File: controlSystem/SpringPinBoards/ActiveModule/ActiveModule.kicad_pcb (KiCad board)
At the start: 2 copper layers, 18.7 x 13.3 mm, 9 parts, among them J1 Conn_01x01_Male, J2 Conn_01x01_Male, J3 Conn_01x01_Male, J4 Conn_01x01_Male, J5 Conn_01x01_Male, J6 Conn_01x01_Male, J7 Conn_01x06

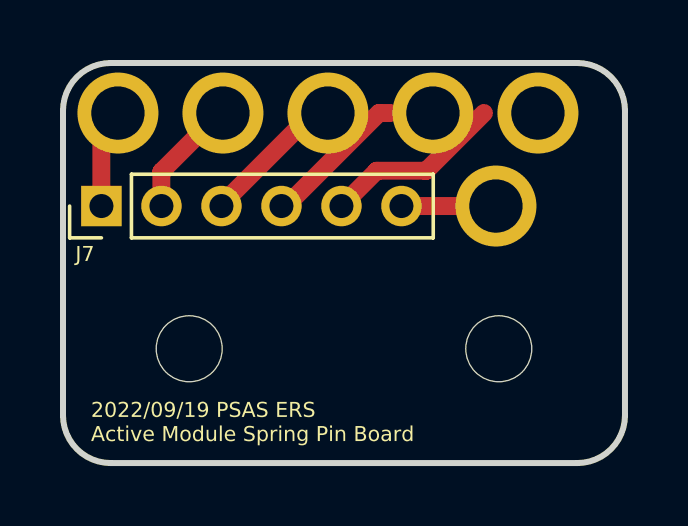
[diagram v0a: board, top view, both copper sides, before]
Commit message: Widened traces on the spring pin boards
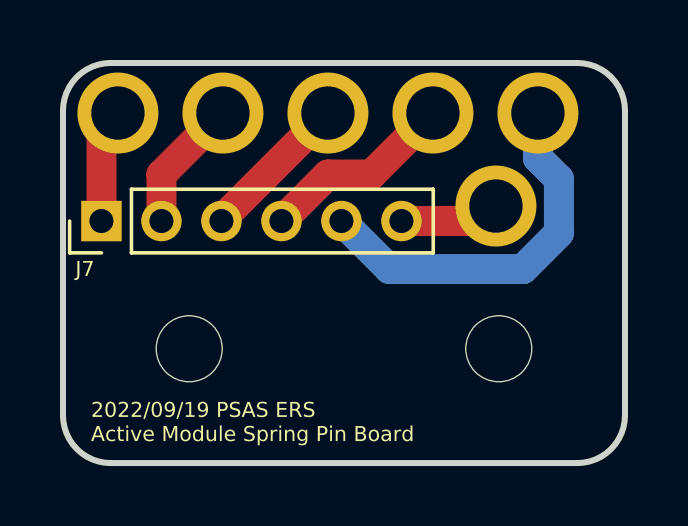
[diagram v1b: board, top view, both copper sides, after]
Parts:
- moved J7 0.50 mm to (141.2, 74.4)
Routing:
- net Net-(J5-Pad1): track 6.03 -> 12.7 mm
- net Net-(J4-Pad1): track 4.93 -> 6.54 mm
- net Net-(J3-Pad1): track 4.16 -> 5.07 mm
- net Net-(J2-Pad1): track 3.70 -> 4.45 mm
- net Net-(J1-Pad1): track 3.24 -> 3.83 mm
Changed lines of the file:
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@@
   (net 6 "Net-(J6-Pad1)")
   (footprint "Connector_PinHeader_2.00mm:PinHeader_1x06_P2.00mm_Vertical" (layer "F.Cu")
-    (at 141.25 73.9 90)
+    (at 141.25 74.4 90)
     (descr "Through hole straight pin header, 1x06, 2.00mm pitch, single row")
     (tags "Through hole pin header THT 1x06 2.00mm single row")
@@
     (effects (font (size 0.5 0.5) (thickness 0.12)) (justify left))
   )
-  (segment (start 141.25 73.9) (end 141.25 71.15) (width 0.6) (layer "F.Cu") (net 1))
-  (segment (start 141.25 71.15) (end 141.6 70.8) (width 0.6) (layer "F.Cu") (net 1))
-  (segment (start 143.25 72.75) (end 144.7 71.3) (width 0.6) (layer "F.Cu") (net 2))
-  (segment (start 143.25 73.9) (end 143.25 72.75) (width 0.6) (layer "F.Cu") (net 2))
-  (segment (start 144.7 71.3) (end 144.7 70.8) (width 0.6) (layer "F.Cu") (net 2))
-  (segment (start 147.8 71.3) (end 147.8 70.8) (width 0.6) (layer "F.Cu") (net 3))
-  (segment (start 145.25 73.85) (end 147.8 71.3) (width 0.6) (layer "F.Cu") (net 3))
-  (segment (start 145.25 73.9) (end 145.25 73.85) (width 0.6) (layer "F.Cu") (net 3))
-  (segment (start 147.25 73.9) (end 147.4 73.9) (width 0.6) (layer "F.Cu") (net 4))
-  (segment (start 150.5 70.8) (end 150.9 70.8) (width 0.6) (layer "F.Cu") (net 4))
-  (segment (start 147.4 73.9) (end 150.5 70.8) (width 0.6) (layer "F.Cu") (net 4))
-  (segment (start 149.25 73.9) (end 150.425 72.725) (width 0.6) (layer "F.Cu") (net 5))
-  (segment (start 152.075 72.725) (end 154 70.8) (width 0.6) (layer "F.Cu") (net 5))
-  (segment (start 150.425 72.725) (end 152.075 72.725) (width 0.6) (layer "F.Cu") (net 5))
-  (segment (start 151.25 73.9) (end 154.4 73.9) (width 0.6) (layer "F.Cu") (net 6))
+  (segment (start 141.25 71.35) (end 141.8 70.8) (width 1) (layer "F.Cu") (net 1))
+  (segment (start 141.25 74.4) (end 141.25 71.35) (width 1) (layer "F.Cu") (net 1))
+  (segment (start 143.25 72.85) (end 145.3 70.8) (width 1) (layer "F.Cu") (net 2))
+  (segment (start 143.25 74.4) (end 143.25 72.85) (width 1) (layer "F.Cu") (net 2))
+  (segment (start 145.25 74.4) (end 145.25 74.35) (width 1) (layer "F.Cu") (net 3))
+  (segment (start 145.25 74.35) (end 148.8 70.8) (width 1) (layer "F.Cu") (net 3))
+  (segment (start 148.8 72.85) (end 150.25 72.85) (width 1) (layer "F.Cu") (net 4))
+  (segment (start 147.25 74.4) (end 148.8 72.85) (width 1) (layer "F.Cu") (net 4))
+  (segment (start 150.25 72.85) (end 152.3 70.8) (width 1) (layer "F.Cu") (net 4))
+  (segment (start 150.85 76) (end 155.3 76) (width 1) (layer "B.Cu") (net 5))
+  (segment (start 155.3 76) (end 156.5 74.8) (width 1) (layer "B.Cu") (net 5))
+  (segment (start 156.5 74.8) (end 156.5 73) (width 1) (layer "B.Cu") (net 5))
+  (segment (start 155.8 72.3) (end 155.8 70.8) (width 1) (layer "B.Cu") (net 5))
+  (segment (start 156.5 73) (end 155.8 72.3) (width 1) (layer "B.Cu") (net 5))
+  (segment (start 149.25 74.4) (end 150.85 76) (width 1) (layer "B.Cu") (net 5))
+  (segment (start 151.25 74.4) (end 153.9 74.4) (width 1) (layer "F.Cu") (net 6))
+  (segment (start 153.9 74.4) (end 154.4 73.9) (width 1) (layer "F.Cu") (net 6))
   (group "" (id 67053cc4-faed-4cf5-96b7-90713502d4d0)
     (members

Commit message: Moved spring pin board libraries to psas-kicad
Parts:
- J1, J2, J3, J4, J5, J6: footprint Mill-Max-0921-5-15-20-77-14-11-0:0921-5-15-20-77-14-11-0 -> psas-footprints:Mill-Max-0921-5-15-20-77-14-11-0
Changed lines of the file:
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@@
     (pad "" np_thru_hole circle (at 0 0) (size 2.2 2.2) (drill 2.2) (layers *.Cu *.Mask))
   )
-  (footprint "Mill-Max-0921-5-15-20-77-14-11-0:0921-5-15-20-77-14-11-0" (layer "F.Cu")
+  (footprint "psas-footprints:Mill-Max-0921-5-15-20-77-14-11-0" (layer "F.Cu")
     (at 154.4 73.9)
     (property "Sheetfile" "ActiveModule.kicad_sch")
@@
       (rotate (xyz 0 90 0))
     )
+    (model "${PSAS_LIBRARIES}/psas-3dmodels/mill-max-0921-5-15-20-77-14-11-0 .step"
+      (offset (xyz 0 0 -3.5))
+      (scale (xyz 1 1 1))
+      (rotate (xyz 0 90 0))
+    )
   )
-  (footprint "Mill-Max-0921-5-15-20-77-14-11-0:0921-5-15-20-77-14-11-0" (layer "F.Cu")
+  (footprint "psas-footprints:Mill-Max-0921-5-15-20-77-14-11-0" (layer "F.Cu")
     (at 148.8 70.8)
     (property "Sheetfile" "ActiveModule.kicad_sch")
@@
       (rotate (xyz 0 90 0))
     )
+    (model "${PSAS_LIBRARIES}/psas-3dmodels/mill-max-0921-5-15-20-77-14-11-0 .step"
+      (offset (xyz 0 0 -3.5))
+      (scale (xyz 1 1 1))
+      (rotate (xyz 0 90 0))
+    )
   )
-  (footprint "Mill-Max-0921-5-15-20-77-14-11-0:0921-5-15-20-77-14-11-0" (layer "F.Cu")
+  (footprint "psas-footprints:Mill-Max-0921-5-15-20-77-14-11-0" (layer "F.Cu")
     (at 141.8 70.8)
     (property "Sheetfile" "ActiveModule.kicad_sch")
@@
       (rotate (xyz 0 90 0))
     )
+    (model "${PSAS_LIBRARIES}/psas-3dmodels/mill-max-0921-5-15-20-77-14-11-0 .step"
+      (offset (xyz 0 0 -3.5))
+      (scale (xyz 1 1 1))
+      (rotate (xyz 0 90 0))
+    )
   )
-  (footprint "Mill-Max-0921-5-15-20-77-14-11-0:0921-5-15-20-77-14-11-0" (layer "F.Cu")
+  (footprint "psas-footprints:Mill-Max-0921-5-15-20-77-14-11-0" (layer "F.Cu")
     (at 145.3 70.8)
     (property "Sheetfile" "ActiveModule.kicad_sch")
@@
       (rotate (xyz 0 90 0))
     )
+    (model "${PSAS_LIBRARIES}/psas-3dmodels/mill-max-0921-5-15-20-77-14-11-0 .step"
+      (offset (xyz 0 0 -3.5))
+      (scale (xyz 1 1 1))
+      (rotate (xyz 0 90 0))
+    )
   )
-  (footprint "Mill-Max-0921-5-15-20-77-14-11-0:0921-5-15-20-77-14-11-0" (layer "F.Cu")
+  (footprint "psas-footprints:Mill-Max-0921-5-15-20-77-14-11-0" (layer "F.Cu")
     (at 152.3 70.8)
     (property "Sheetfile" "ActiveModule.kicad_sch")
@@
       (rotate (xyz 0 90 0))
     )
+    (model "${PSAS_LIBRARIES}/psas-3dmodels/mill-max-0921-5-15-20-77-14-11-0 .step"
+      (offset (xyz 0 0 -3.5))
+      (scale (xyz 1 1 1))
+      (rotate (xyz 0 90 0))
+    )
   )
-  (footprint "Mill-Max-0921-5-15-20-77-14-11-0:0921-5-15-20-77-14-11-0" (layer "F.Cu")
+  (footprint "psas-footprints:Mill-Max-0921-5-15-20-77-14-11-0" (layer "F.Cu")
     (at 155.8 70.8)
     (property "Sheetfile" "ActiveModule.kicad_sch")
@@
       (offset (xyz 0 0 -3.5))
       (scale (xyz 1 1 1))
+      (rotate (xyz 0 90 0))
+    )
+    (model "${PSAS_LIBRARIES}/psas-3dmodels/mill-max-0921-5-15-20-77-14-11-0 .step"
+      (offset (xyz 0 0 -3.5))
+      (scale (xyz 1 1 1))
